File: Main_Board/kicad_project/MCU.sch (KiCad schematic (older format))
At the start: 11 parts

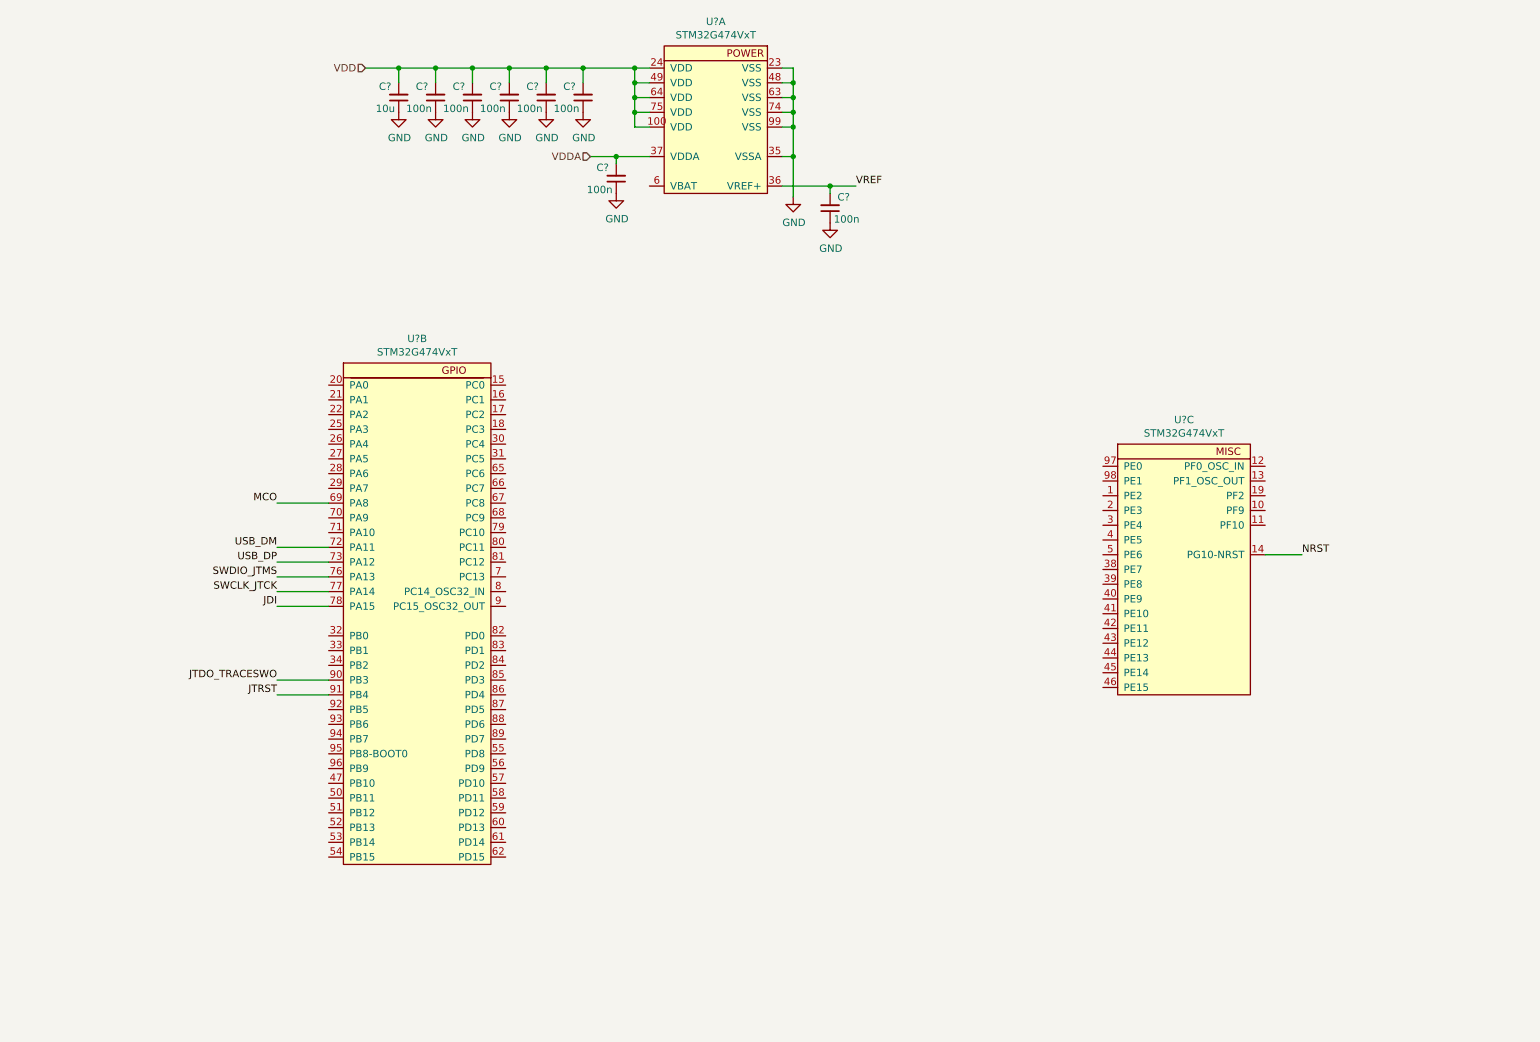
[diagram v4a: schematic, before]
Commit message: more progress on MCU pinout
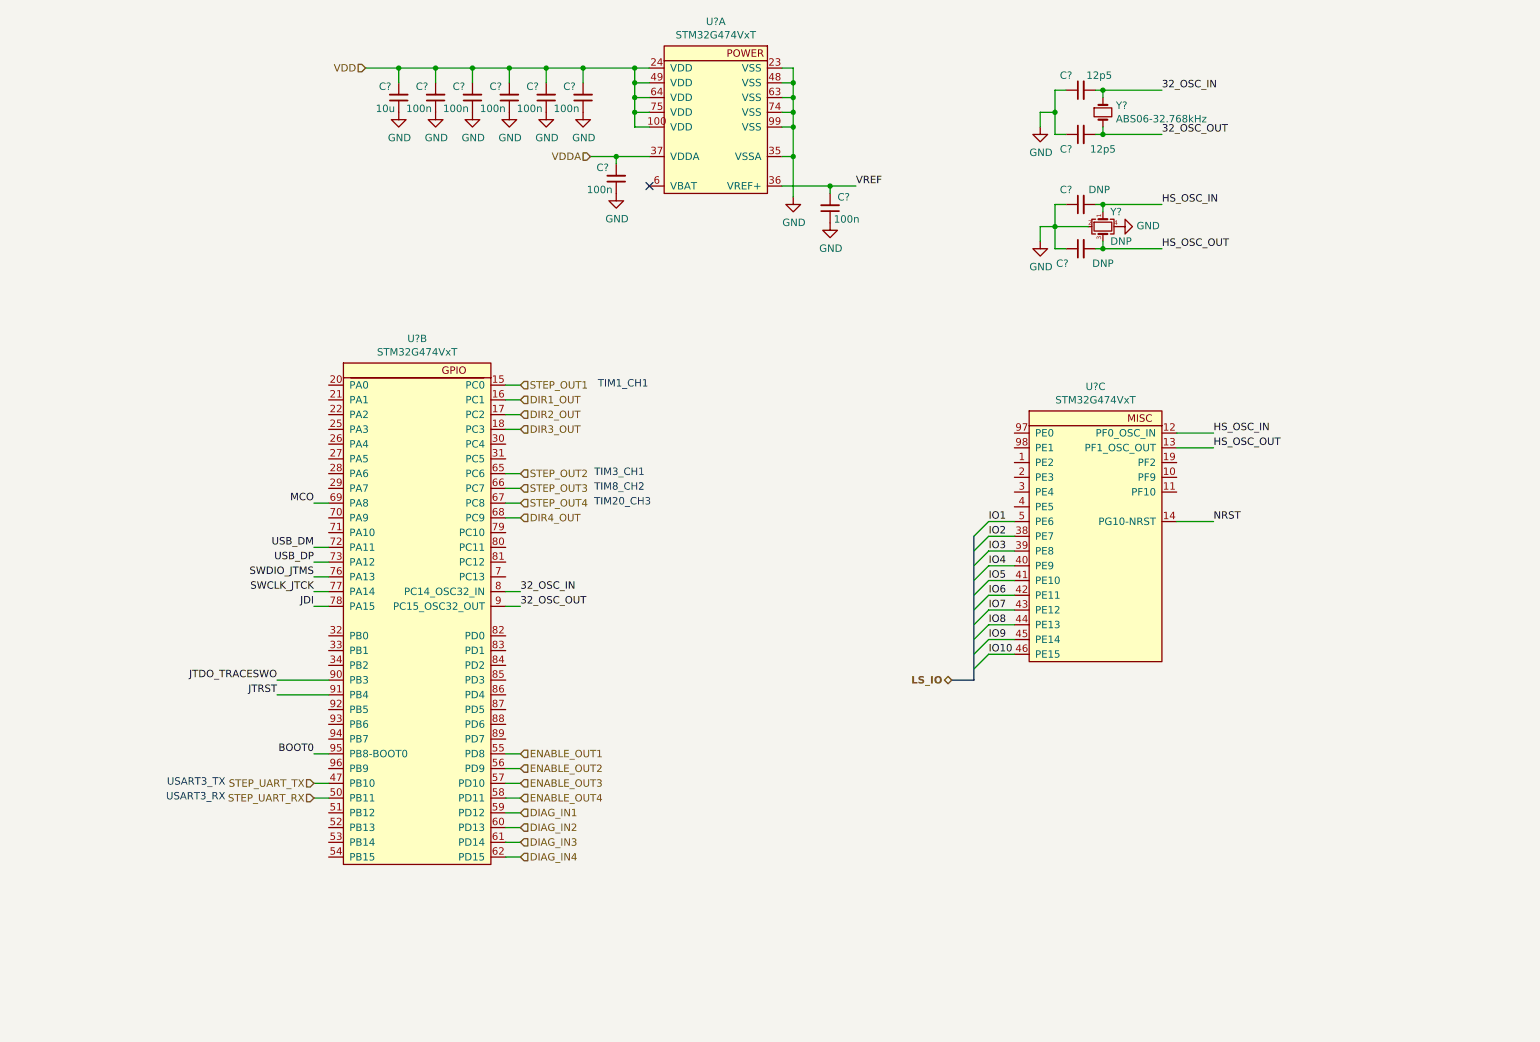
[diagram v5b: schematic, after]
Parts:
- added C? (x2): DNP, Capacitor_SMD:C_0603_1608Metric, symbol Device:C_Small
- added C? (x2): 12p5, Capacitor_SMD:C_0603_1608Metric, symbol Device:C_Small
- added Y?: DNP, Crystal:Crystal_SMD_2016-4Pin_2.0x1.6mm, symbol Device:Crystal_GND24_Small
- added Y?: ABS06-32.768kHz, Crystal:Crystal_SMD_2012-2Pin_2.0x1.2mm, symbol Device:Crystal_Small
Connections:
- net GND: now also C?.1, C?.1, C?.1, C?.1, Y?.2, Y?.4
- net STEP_OUT1: now reaches U?.15 (PC0)
- net DIR1_OUT: now reaches U?.16 (PC1)
- net DIR2_OUT: now reaches U?.17 (PC2)
- net DIR3_OUT: now reaches U?.18 (PC3)
- net STEP_UART_TX: now reaches U?.47 (PB10)
- net STEP_UART_RX: now reaches U?.50 (PB11)
- net ENABLE_OUT1: now reaches U?.55 (PD8)
- net ENABLE_OUT2: now reaches U?.56 (PD9)
- net ENABLE_OUT3: now reaches U?.57 (PD10)
- net ENABLE_OUT4: now reaches U?.58 (PD11)
- net DIAG_IN1: now reaches U?.59 (PD12)
- net DIAG_IN2: now reaches U?.60 (PD13)
- net DIAG_IN3: now reaches U?.61 (PD14)
- net DIAG_IN4: now reaches U?.62 (PD15)
- net STEP_OUT2: now reaches U?.65 (PC6)
- net STEP_OUT3: now reaches U?.66 (PC7)
- net STEP_OUT4: now reaches U?.67 (PC8)
- net DIR4_OUT: now reaches U?.68 (PC9)
- net 32_OSC_IN: now reaches U?.8 (PC14_OSC32_IN)
- net 32_OSC_IN: now also C?.2, Y?.1
- net 32_OSC_OUT: now reaches U?.9 (PC15_OSC32_OUT)
- net 32_OSC_OUT: now also C?.2, Y?.2
- net BOOT0: now reaches U?.95 (PB8-BOOT0)
- net HS_OSC_IN: now reaches U?.12 (PF0_OSC_IN)
- net HS_OSC_IN: now also C?.2, Y?.1
- net HS_OSC_OUT: now reaches U?.13 (PF1_OSC_OUT)
- net HS_OSC_OUT: now also C?.2, Y?.3
- net IO2: now reaches U?.38 (PE7)
- net IO3: now reaches U?.39 (PE8)
- net IO4: now reaches U?.40 (PE9)
- net IO5: now reaches U?.41 (PE10)
- net IO6: now reaches U?.42 (PE11)
- net IO7: now reaches U?.43 (PE12)
- net IO8: now reaches U?.44 (PE13)
- net IO9: now reaches U?.45 (PE14)
- net IO10: now reaches U?.46 (PE15)
- net IO1: now reaches U?.5 (PE6)
- no-connect marks 0 -> 1
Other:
- note added: "TIM1_CH1"
- note added: "TIM20_CH3"
- note added: "TIM3_CH1"
- note added: "TIM8_CH2"
- note added: "USART3_RX"
- note added: "USART3_TX"
- moved on the sheet: U?C

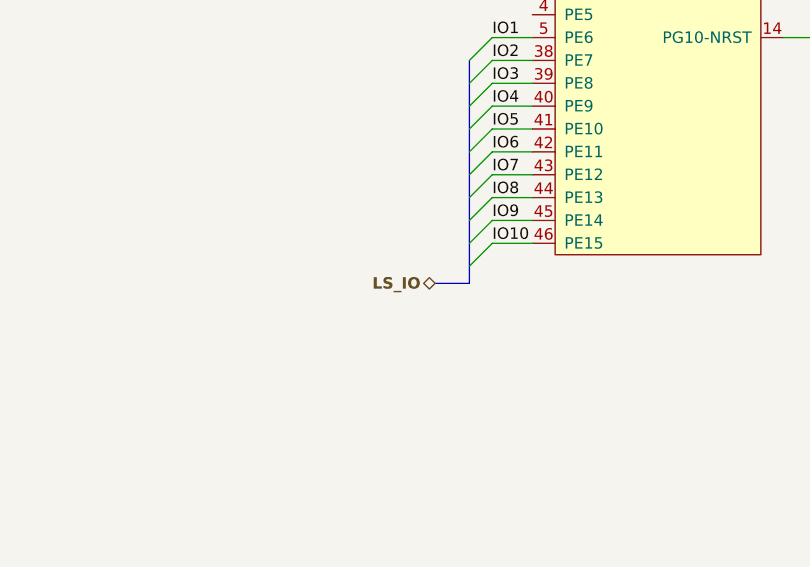
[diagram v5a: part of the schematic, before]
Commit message: fix bus connection
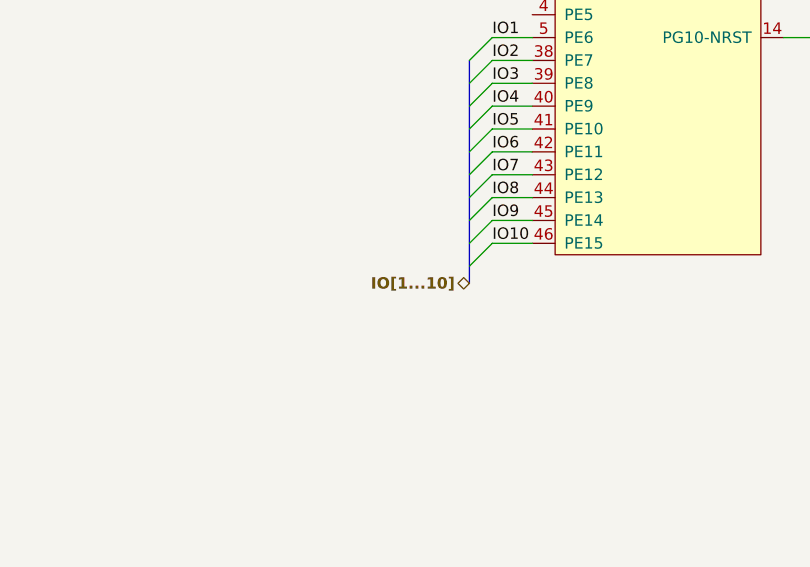
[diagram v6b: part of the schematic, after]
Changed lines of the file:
@@
 $Descr A4 11693 8268
 encoding utf-8
-Sheet 7 9
+Sheet 8 9
 Title ""
 Date ""
@@
 Entry Wire Line
 	7325 4825 7225 4925
-Wire Bus Line
-	7225 5000 7075 5000
-Text HLabel 7075 5000 0    50   BiDi ~ 10
-LS_IO
 Text Label 7325 3925 0    50   ~ 0
 IO1
@@
 Wire Bus Line
 	7225 4025 7225 5000
+Text HLabel 7225 5000 0    50   BiDi ~ 10
+IO[1...10]
 $EndSCHEMATC

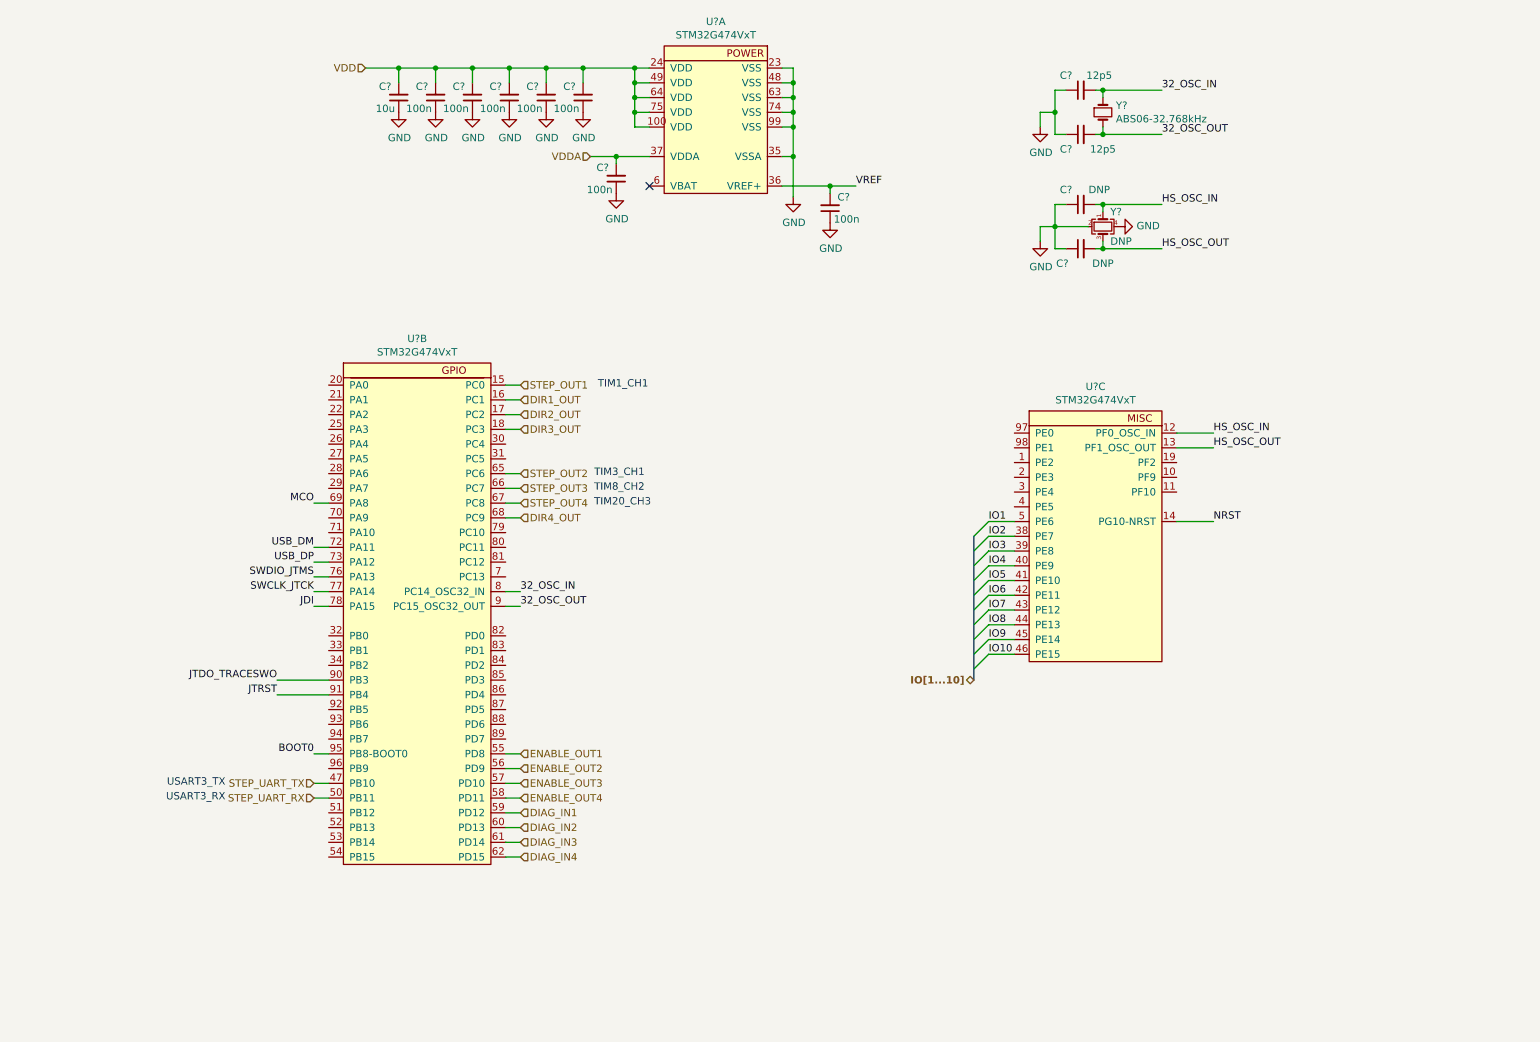
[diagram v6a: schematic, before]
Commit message: MCU pinout done
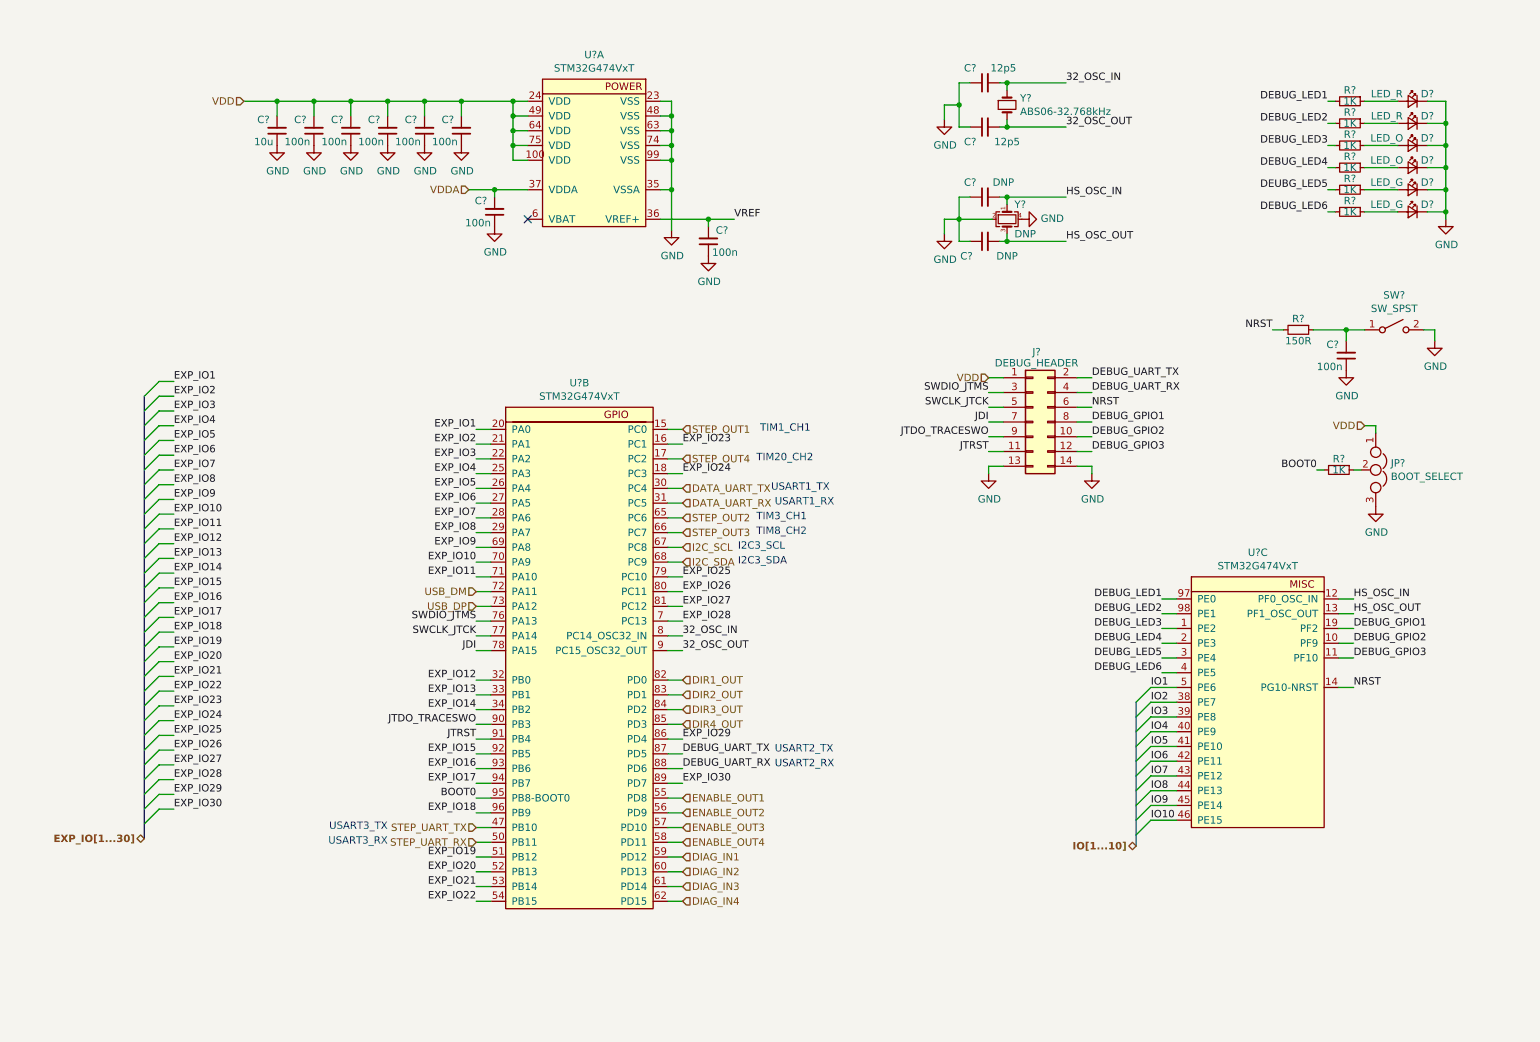
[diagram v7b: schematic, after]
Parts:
- added C?: 100n, Capacitor_SMD:C_0603_1608Metric, symbol Device:C_Small
- added D? (x2): LED_R, Diode_SMD:D_0603_1608Metric, symbol Device:LED_Small
- added D? (x2): LED_O, Diode_SMD:D_0603_1608Metric, symbol Device:LED_Small
- added D? (x2): LED_G, Diode_SMD:D_0603_1608Metric, symbol Device:LED_Small
- added J?: DEBUG_HEADER, Connector_PinHeader_2.54mm:PinHeader_2x07_P2.54mm_Vertical, symbol Connector_Generic:Conn_02x07_Odd_Even
- added JP?: BOOT_SELECT, Connector_PinHeader_2.54mm:PinHeader_1x03_P2.54mm_Vertical, symbol Device:Jumper_NC_Dual
- added R? (x7): 1K, Resistor_SMD:R_0603_1608Metric, symbol Device:R_Small
- added R?: 150R, Resistor_SMD:R_0603_1608Metric, symbol Device:R_Small
- added SW?: SW_SPST, Button_Switch_THT:SW_PUSH_6mm_H5mm, symbol Switch:SW_SPST
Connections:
- net BOOT0: now also R?.2
- net DIR1_OUT: now also U?.82 (PD0); no longer U?.16 (PC1)
- net DIR2_OUT: now also U?.83 (PD1); no longer U?.17 (PC2)
- net DIR3_OUT: now also U?.84 (PD2); no longer U?.18 (PC3)
- net DIR4_OUT: now also U?.85 (PD3); no longer U?.68 (PC9)
- net GND: now also C?.1, D?.1 (K), D?.1 (K), D?.1 (K), D?.1 (K), D?.1 (K), D?.1 (K), J?.13 (Pin_13), J?.14 (Pin_14), JP?.3, SW?.2 (B)
- net JDI: now also J?.7 (Pin_7)
- net JTDO_TRACESWO: now also J?.9 (Pin_9)
- net JTRST: now also J?.11 (Pin_11)
- net NRST: now also J?.6 (Pin_6), R?.2
- net STEP_OUT4: now also U?.17 (PC2); no longer U?.67 (PC8)
- net SWCLK_JTCK: now also J?.5 (Pin_5)
- net SWDIO_JTMS: now also J?.3 (Pin_3)
- net VDD: now also J?.1 (Pin_1), JP?.1
- net EXP_IO1: now reaches U?.20 (PA0)
- net EXP_IO2: now reaches U?.21 (PA1)
- net EXP_IO3: now reaches U?.22 (PA2)
- net EXP_IO4: now reaches U?.25 (PA3)
- net EXP_IO5: now reaches U?.26 (PA4)
- net EXP_IO6: now reaches U?.27 (PA5)
- net EXP_IO7: now reaches U?.28 (PA6)
- net EXP_IO8: now reaches U?.29 (PA7)
- net DATA_UART_TX: now reaches U?.30 (PC4)
- net DATA_UART_RX: now reaches U?.31 (PC5)
- net EXP_IO12: now reaches U?.32 (PB0)
- net EXP_IO13: now reaches U?.33 (PB1)
- net EXP_IO14: now reaches U?.34 (PB2)
- net EXP_IO19: now reaches U?.51 (PB12)
- net EXP_IO20: now reaches U?.52 (PB13)
- net EXP_IO21: now reaches U?.53 (PB14)
- net EXP_IO22: now reaches U?.54 (PB15)
- net EXP_IO28: now reaches U?.7 (PC13)
- net EXP_IO10: now reaches U?.70 (PA9)
- net EXP_IO11: now reaches U?.71 (PA10)
- net EXP_IO25: now reaches U?.79 (PC10)
- net EXP_IO26: now reaches U?.80 (PC11)
- net EXP_IO27: now reaches U?.81 (PC12)
- net EXP_IO29: now reaches U?.86 (PD4)
- net DEBUG_UART_TX: now reaches U?.87 (PD5)
- net DEBUG_UART_TX: now also J?.2 (Pin_2)
- net DEBUG_UART_RX: now reaches U?.88 (PD6)
- net DEBUG_UART_RX: now also J?.4 (Pin_4)
- net EXP_IO30: now reaches U?.89 (PD7)
- net EXP_IO15: now reaches U?.92 (PB5)
- net EXP_IO16: now reaches U?.93 (PB6)
- net EXP_IO17: now reaches U?.94 (PB7)
- net EXP_IO18: now reaches U?.96 (PB9)
- net DEBUG_LED3: now reaches U?.1 (PE2)
- net DEBUG_LED3: now also R?.2
- net DEBUG_GPIO2: now reaches U?.10 (PF9)
- net DEBUG_GPIO2: now also J?.10 (Pin_10)
- net DEBUG_GPIO3: now reaches U?.11 (PF10)
- net DEBUG_GPIO3: now also J?.12 (Pin_12)
- net DEBUG_GPIO1: now reaches U?.19 (PF2)
- net DEBUG_GPIO1: now also J?.8 (Pin_8)
- net DEBUG_LED4: now reaches U?.2 (PE3)
- net DEBUG_LED4: now also R?.2
- net DEUBG_LED5: now reaches U?.3 (PE4)
- net DEUBG_LED5: now also R?.2
- net DEBUG_LED6: now reaches U?.4 (PE5)
- net DEBUG_LED6: now also R?.2
- net DEBUG_LED1: now reaches U?.97 (PE0)
- net DEBUG_LED1: now also R?.2
- net DEBUG_LED2: now reaches U?.98 (PE1)
- net DEBUG_LED2: now also R?.2
- net MCO renamed EXP_IO9
- new net: D?.2 (A), R?.1 (x6)
- new net: C?.2, R?.1, SW?.1 (A)
- new net: JP?.2, R?.1
- new net EXP_IO23: U?.16 (PC1)
- new net EXP_IO24: U?.18 (PC3)
- new net I2C_SCL: U?.67 (PC8)
- new net I2C_SDA: U?.68 (PC9)
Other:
- note added: "I2C3_SCL"
- note added: "I2C3_SDA"
- note added: "TIM20_CH2"
- note added: "USART1_RX"
- note added: "USART1_TX"
- note added: "USART2_RX"
- note added: "USART2_TX"
- note removed: "TIM20_CH3"
- moved on the sheet: C?, U?A, U?B, U?C, Y?

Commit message: schematic rev1 finished
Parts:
- gave numbers to parts that had none: 33
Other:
- note added: "32.768kHz oscillator and\noptional HSE oscillator for MCU"
- note added: "Boot select jumper"
- note added: "Both should be placed very close to MCU\nLayout is important!!"
- note added: "Debug header"
- note added: "Each VDD/VSS pair gets a 100n capacitor.\nCapacitor should be placed as close as possible to the pins."
- note added: "Expansion bus entry"
- note added: "MCU Power"
- note added: "MCU and debug connections"
- note added: "Reset button"
- note added: "debug/status LEDs"
- moved on the sheet: C56, C57, C58, C59, C60, C61, C62, C63, C64, C65, C66, C67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
